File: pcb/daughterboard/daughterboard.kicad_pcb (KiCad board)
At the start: 2 copper layers, 220 x 50 mm, 71 parts, among them IC1 TLE94112ESXUMA1, IC2 TLE94112ESXUMA1, IC3 TLE94112ESXUMA1, IC4 TLE94112ESXUMA1, IC5 TLE94112ESXUMA1, IC6 TLE94112ESXUMA1, IC7 TLE94112ESXUMA1, J10 Conn_01x06_Socket, J11 Conn_01x06_Socket, J12 Conn_01x06_Socket, J13 Conn_01x06_Socket, J14 Conn_01x06_Socket, J15 Conn_01x06_Socket, J16 Conn_01x06_Socket, J17 Conn_01x06_Socket, J18 Conn_01x06_Socket, J19 Conn_01x06_Socket, J2 M20-7820646, J20 Conn_01x06_Socket, J21 Conn_01x06_Socket, J22 Conn_01x06_Socket, J23 Screw_Terminal_01x03, J3 Conn_01x06_Socket, J4 Conn_01x06_Socket, J5 Conn_01x06_Socket, J6 Conn_01x06_Socket, J7 Conn_01x06_Socket, J8 Conn_01x06_Socket, J9 Conn_01x06_Socket

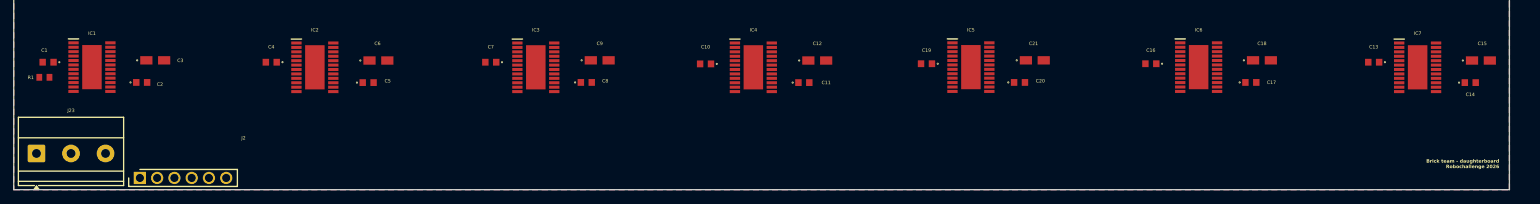
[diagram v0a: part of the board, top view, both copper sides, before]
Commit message: added power lines
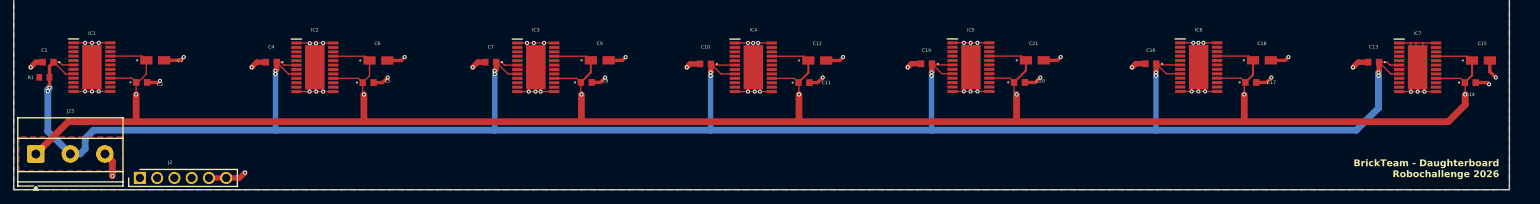
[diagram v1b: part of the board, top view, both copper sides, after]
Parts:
- moved J23 0.12 mm to (35.4, 147.3)
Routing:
- net +5.5V: track 0.00 -> 347.1 mm, vias 0 -> 7
- net +3.3V: track 0.00 -> 317.2 mm, vias 0 -> 14
- net GND: track 0.00 -> 298.4 mm, vias 0 -> 62
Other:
- board text added: "BrickTeam - Daughterboard Robochallenge 2026"
- board text removed: "Brick team - daughterboard Robochallenge 2026"

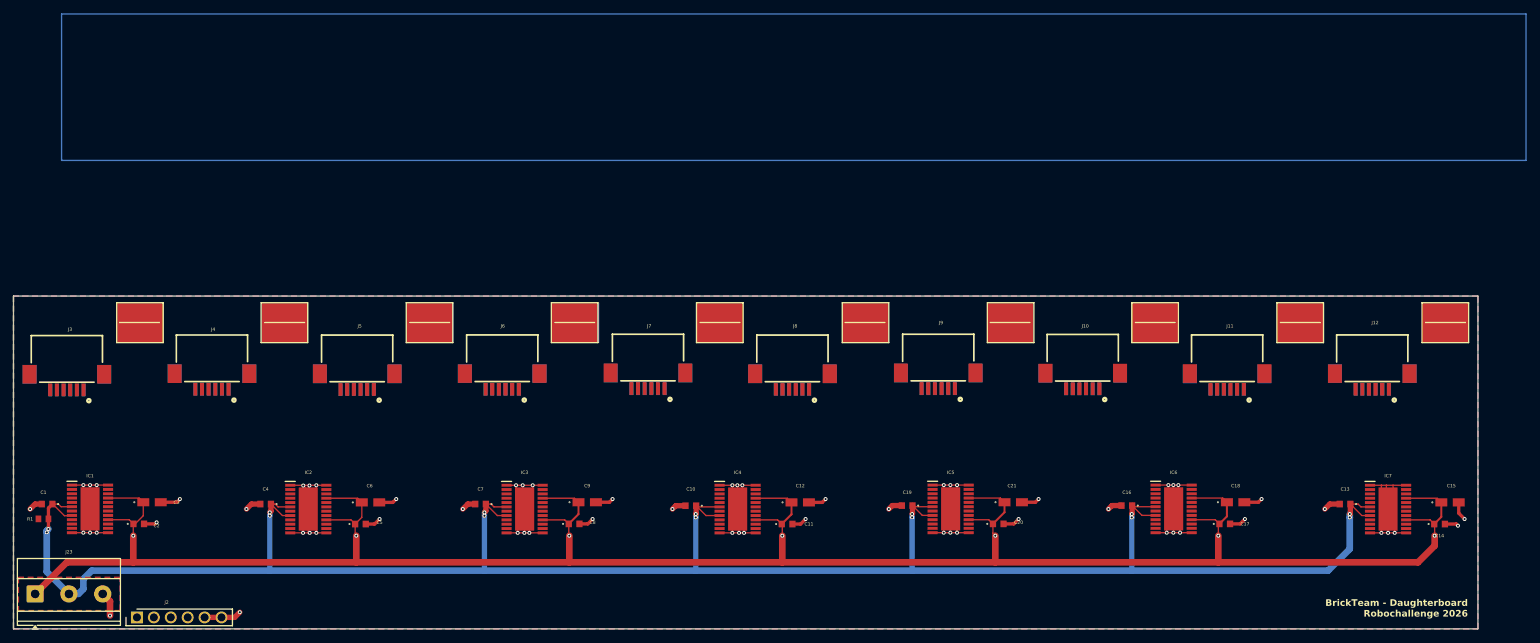
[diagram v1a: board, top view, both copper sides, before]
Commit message: Routed 10 motors and realised daisy-chain connection between drivers
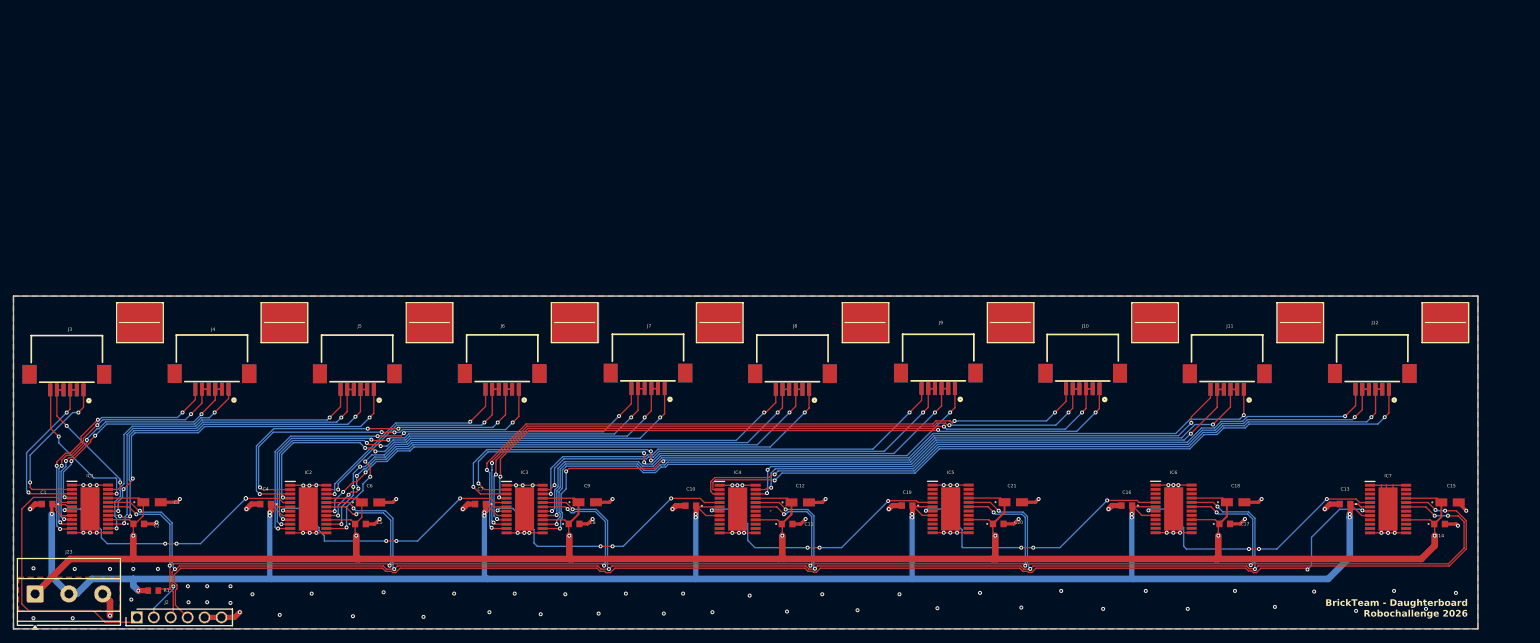
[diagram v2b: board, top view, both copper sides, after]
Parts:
- moved R1 19.7 mm to (53.1, 146.8), turned to 0 degrees
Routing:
- net /drivers1/SPI_SCLK: track 0.00 -> 329.2 mm, vias 0 -> 15
- net /drivers1/SPI_CS: track 0.00 -> 321.9 mm, vias 0 -> 14
- net /drivers2/SPI_MISO: track 0.00 -> 196.8 mm, vias 0 -> 2
- net PAD1_M9: track 0.00 -> 119.0 mm, vias 0 -> 2
- net PAD2_M9: track 0.00 -> 118.3 mm, vias 0 -> 2
- net PAD3_M9: track 0.00 -> 117.5 mm, vias 0 -> 2
- net PAD4_M9: track 0.00 -> 115.1 mm, vias 0 -> 4
- net PAD2_M10: track 0.00 -> 111.7 mm, vias 0 -> 2
- net PAD1_M10: track 0.00 -> 111.6 mm, vias 0 -> 2
- net PAD2_M8: track 0.00 -> 106.8 mm, vias 0 -> 4
- net PAD3_M8: track 0.00 -> 106.1 mm, vias 0 -> 4
- net PAD4_M8: track 0.00 -> 105.3 mm, vias 0 -> 4
- net PAD1_M8: track 0.00 -> 103.3 mm, vias 0 -> 4
- net PAD3_M10: track 0.00 -> 101.5 mm, vias 0 -> 2
- net PAD4_M10: track 0.00 -> 100.1 mm, vias 0 -> 3
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
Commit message: Finalized daughterboard pcb design 0 errors Verified every 3D model, footprint According to the schematic
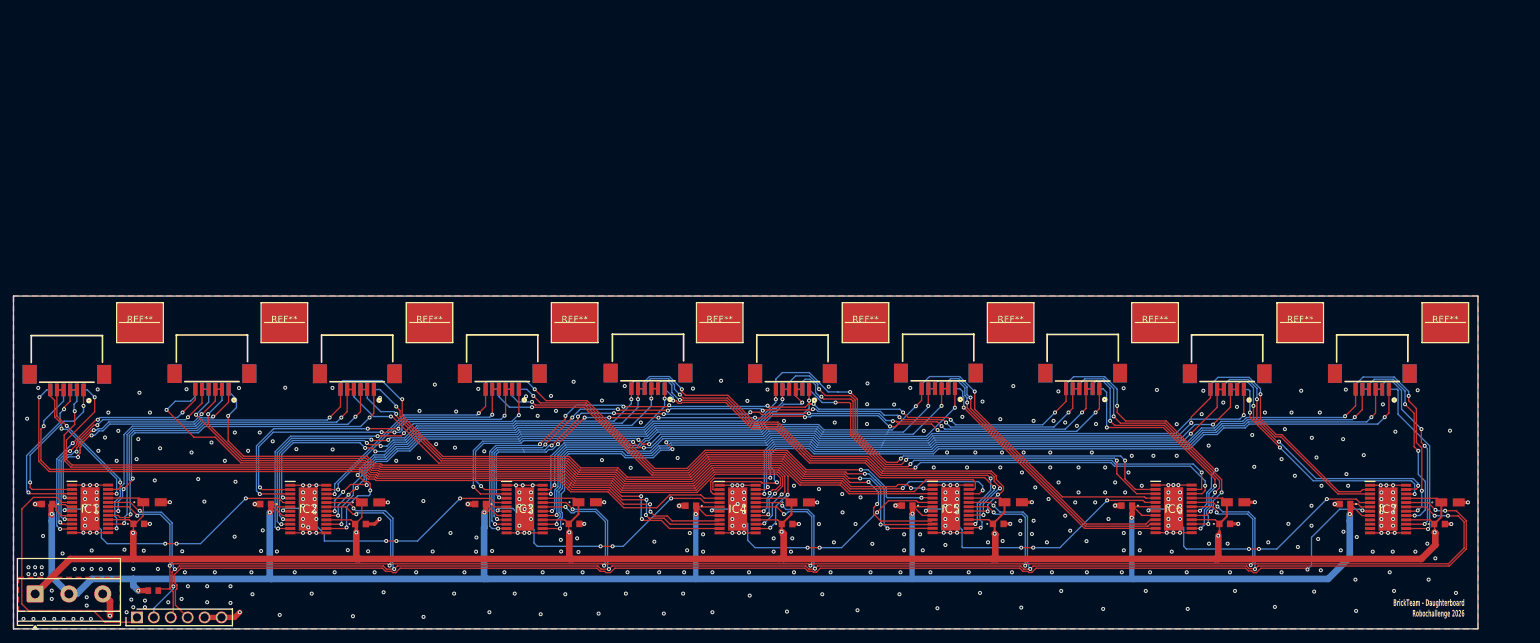
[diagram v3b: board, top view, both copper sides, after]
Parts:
- removed the ? at (160.1, 106.6) (x2)
- removed the ? at (247.2, 106.6)
- removed the ? at (225.5, 106.6)
- removed the ? at (247.3, 106.6)
- removed the ? at (116.6, 106.6)
- removed the ? at (203.7, 106.6)
- removed the ? at (181.9, 106.6) (x2)
- removed the ? at (94.7, 106.6)
- removed the ? at (138.3, 106.6)
- removed the ? at (72.8, 106.6)
- removed the ? at (72.9, 106.6)
- removed the REF** at (51.1, 106.6)
- added ?: , , F.Cu at (51.1, 106.6)
- added ?: , , F.Cu at (160.1, 106.6)
- added ?: , , F.Cu at (181.9, 106.6)
- added ?: , , F.Cu at (72.8, 106.6)
- added REF**: 6x7mm_F_pad, daughterboard:7x6mm_F_pad, F.Cu at (225.4, 106.6)
- added REF**: 6x7mm_F_pad, daughterboard:7x6mm_F_pad, F.Cu at (203.6, 106.6)
- added REF**: 6x7mm_F_pad, daughterboard:7x6mm_F_pad, F.Cu at (51.1, 106.6)
- added REF**: 6x7mm_F_pad, daughterboard:7x6mm_F_pad, F.Cu at (138.2, 106.6)
- added REF**: 6x7mm_F_pad, daughterboard:7x6mm_F_pad, F.Cu at (72.8, 106.6)
- added REF**: 6x7mm_F_pad, daughterboard:7x6mm_F_pad, F.Cu at (160.1, 106.6)
- added REF**: 6x7mm_F_pad, daughterboard:7x6mm_F_pad, F.Cu at (116.4, 106.6)
- added REF**: 6x7mm_F_pad, daughterboard:7x6mm_F_pad, F.Cu at (247.2, 106.6)
- added REF**: 6x7mm_F_pad, daughterboard:7x6mm_F_pad, F.Cu at (181.9, 106.6)
- added REF**: 6x7mm_F_pad, daughterboard:7x6mm_F_pad, F.Cu at (94.6, 106.6)
- IC1, IC2, IC3, IC4, IC5, IC6, IC7: footprint A_HANU_FOOTPRINTS:TLE94112ESXUMA1 -> driver_tle:SOP65P600X115-25N
- moved REF** 196.1 mm to (247.2, 112.3)
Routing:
- net PAD2_M11: track 1.00 -> 119.5 mm, vias 0 -> 3
- net PAD1_M11: track 0.00 -> 117.9 mm, vias 0 -> 1
- net PAD4_M11: track 0.00 -> 117.6 mm, vias 0 -> 3
- net PAD3_M11: track 1.00 -> 116.4 mm, vias 0 -> 3
- net PAD1_M12: track 0.17 -> 112.5 mm, vias 0 -> 3
- net PAD4_M12: track 0.00 -> 108.4 mm, vias 0 -> 3
- net PAD3_M12: track 1.00 -> 109.0 mm, vias 0 -> 3
- net PAD2_M12: track 1.00 -> 108.4 mm, vias 0 -> 3
- net PAD4_M13: track 0.00 -> 104.2 mm, vias 0 -> 3
- net PAD3_M13: track 1.00 -> 104.8 mm, vias 0 -> 1
- net PAD1_M13: track 0.00 -> 100.8 mm, vias 0 -> 3
- net PAD2_M13: track 1.00 -> 97.3 mm, vias 0 -> 1
- net PAD2_M14: track 1.00 -> 80.4 mm, vias 0 -> 3
- net PAD1_M14: track 0.00 -> 78.5 mm, vias 0 -> 3
- net PAD3_M14: track 1.00 -> 78.6 mm, vias 0 -> 3
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
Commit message: Final touches for the PCB order Added MPN, Description, checked footprints and 3D models Finished the BOM
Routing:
- net PAD4_M8: track 108.9 -> 109.6 mm
- net PAD3_M8: track 109.3 -> 109.8 mm
- net GND: vias 450 -> 416
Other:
- board text added: "BRICKTEAM 2026"
- board text removed: "BrickTeam - Daughterboard Robochallenge 2026"

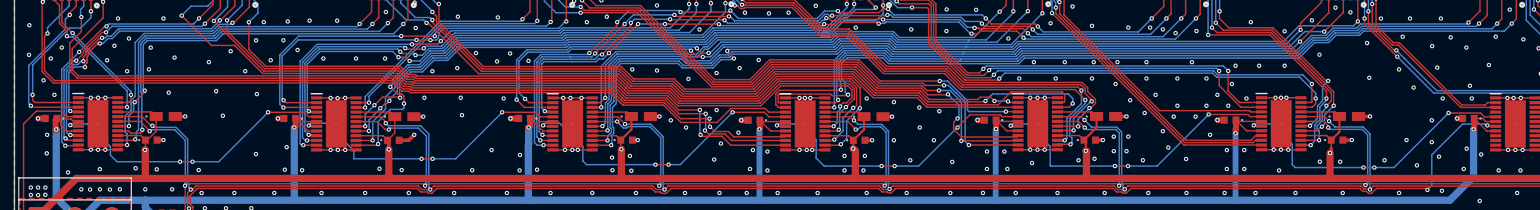
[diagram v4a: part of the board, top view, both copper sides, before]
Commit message: fixed via positioning errors
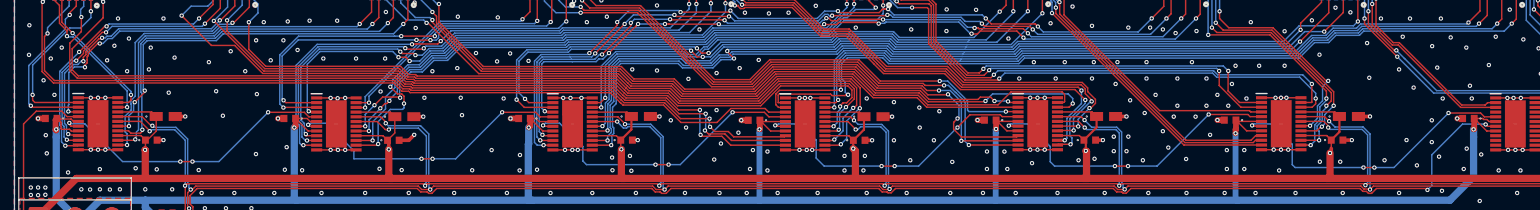
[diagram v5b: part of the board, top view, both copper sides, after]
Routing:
- net PAD2_M5: track 74.3 -> 75.1 mm
- net GND: vias 416 -> 417

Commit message: modified motor connectors
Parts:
- removed the ? at (203.6, 106.6)
- removed the ? at (51.1, 106.6)
- removed the ? at (160.1, 106.6)
- removed the ? at (116.4, 106.6)
- removed the ? at (225.4, 106.6)
- removed the ? at (72.8, 106.6)
- removed J23: Screw_Terminal_01x03, TerminalBlock_Phoenix:TerminalBlock_Phoenix_MKDS-1,5-3-5.08_1x03_P5.08mm_Horizontal
- removed the REF** at (225.4, 106.6)
- removed the REF** at (203.6, 106.6)
- removed the REF** at (138.2, 106.6)
- removed the REF** at (72.8, 106.6)
- removed the REF** at (160.1, 106.6)
- removed the REF** at (116.4, 106.6)
- removed the REF** at (247.2, 106.6)
- removed the REF** at (181.9, 106.6)
- removed the REF** at (94.6, 106.6)
- added ?: , , F.Cu at (181.8, 106.6)
- added ? (x2): , , F.Cu at (72.8, 106.6)
- added ?: , , F.Cu at (94.6, 106.6)
- added ? (x2): , , F.Cu at (203.6, 106.6)
- added ? (x2): , , F.Cu at (116.4, 106.6)
- added ? (x2): , , F.Cu at (160.1, 106.6)
- added ?: , , F.Cu at (51.0, 106.6)
- added ? (x2): , , F.Cu at (225.4, 106.6)
- added ?: , , F.Cu at (138.3, 106.6)
- added ?: , , F.Cu at (247.2, 106.6)
- added J1: Screw_Terminal_01x03, TerminalBlock_Phoenix:TerminalBlock_Phoenix_MKDS-1,5-3-5.08_1x03_P5.08mm_Horizontal, F.Cu at (35.3, 147.3)
- J10, J11, J12, J13, J14, J15, J16, J17, J18, J19, J20, J21, J22, J3, J4, J5, J6, J7, J8, J9: value Conn_01x06_Socket -> FFC3B11-06-T; footprint 52207-0633:52207-0633 -> FFC3B11_06_T:GCT_FFC3B11-06-T
- moved J10 2.85 mm to (192.7, 113.7)
- moved J11 2.85 mm to (214.4, 113.8)
- moved J12 2.85 mm to (236.2, 113.8)
- moved J13 2.85 mm to (40.1, 113.8)
- moved J14 2.85 mm to (61.9, 113.8)
- moved J15 2.85 mm to (83.7, 113.8)
- moved J16 2.85 mm to (105.5, 113.8)
- moved J17 2.85 mm to (127.4, 113.7)
- moved J18 2.85 mm to (149.1, 113.8)
- moved J19 2.85 mm to (171.0, 113.7)
- moved J20 2.85 mm to (192.7, 113.7)
- moved J21 2.85 mm to (214.4, 113.8)
- moved J22 2.85 mm to (236.2, 113.8)
- moved J4 2.85 mm to (61.9, 113.8)
- moved J5 2.85 mm to (83.7, 113.8)
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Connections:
- J10 pad 1: PAD1_M8 -> PAD4_M8
- J10 pad 2: PAD2_M8 -> PAD3_M8
- J10 pad 3: PAD2_M8 -> PAD3_M8
- J10 pad 4: PAD3_M8 -> PAD2_M8
- J10 pad 5: PAD3_M8 -> PAD2_M8
- J10 pad 6: PAD4_M8 -> PAD1_M8
- J11 pad 1: PAD1_M9 -> PAD4_M9
- J11 pad 2: PAD2_M9 -> PAD3_M9
- J11 pad 3: PAD2_M9 -> PAD3_M9
- J11 pad 4: PAD3_M9 -> PAD2_M9
- J11 pad 5: PAD3_M9 -> PAD2_M9
- J11 pad 6: PAD4_M9 -> PAD1_M9
- J12 pad 1: PAD1_M10 -> PAD4_M10
- J12 pad 2: PAD2_M10 -> PAD3_M10
- J12 pad 3: PAD2_M10 -> PAD3_M10
- J12 pad 4: PAD3_M10 -> PAD2_M10
- J12 pad 5: PAD3_M10 -> PAD2_M10
- J12 pad 6: PAD4_M10 -> PAD1_M10
- J13 pad 1: PAD1_M11 -> PAD4_M11
- J13 pad 2: PAD2_M11 -> PAD3_M11
- J13 pad 3: PAD2_M11 -> PAD3_M11
- J13 pad 4: PAD3_M11 -> PAD2_M11
- J13 pad 5: PAD3_M11 -> PAD2_M11
- J13 pad 6: PAD4_M11 -> PAD1_M11
- J14 pad 1: PAD1_M12 -> PAD4_M12
- J14 pad 2: PAD2_M12 -> PAD3_M12
- J14 pad 3: PAD2_M12 -> PAD3_M12
- J14 pad 4: PAD3_M12 -> PAD2_M12
- J14 pad 5: PAD3_M12 -> PAD2_M12
- J14 pad 6: PAD4_M12 -> PAD1_M12
- J15 pad 1: PAD1_M13 -> PAD4_M13
- J15 pad 2: PAD2_M13 -> PAD3_M13
- J15 pad 3: PAD2_M13 -> PAD3_M13
- J15 pad 4: PAD3_M13 -> PAD2_M13
- J15 pad 5: PAD3_M13 -> PAD2_M13
- J15 pad 6: PAD4_M13 -> PAD1_M13
- J16 pad 1: PAD1_M14 -> PAD4_M14
- J16 pad 2: PAD2_M14 -> PAD3_M14
- J16 pad 3: PAD2_M14 -> PAD3_M14
- J16 pad 4: PAD3_M14 -> PAD2_M14
- J16 pad 5: PAD3_M14 -> PAD2_M14
- J16 pad 6: PAD4_M14 -> PAD1_M14
- J17 pad 1: PAD1_M15 -> PAD4_M15
- J17 pad 2: PAD2_M15 -> PAD3_M15
- J17 pad 3: PAD2_M15 -> PAD3_M15
- J17 pad 4: PAD3_M15 -> PAD2_M15
- J17 pad 5: PAD3_M15 -> PAD2_M15
- J17 pad 6: PAD4_M15 -> PAD1_M15
- J18 pad 1: PAD1_M16 -> PAD4_M16
- J18 pad 2: PAD2_M16 -> PAD3_M16
- J18 pad 3: PAD2_M16 -> PAD3_M16
- J18 pad 4: PAD3_M16 -> PAD2_M16
- J18 pad 5: PAD3_M16 -> PAD2_M16
- J18 pad 6: PAD4_M16 -> PAD1_M16
- J19 pad 1: PAD1_M17 -> PAD4_M17
- J19 pad 2: PAD2_M17 -> PAD3_M17
- J19 pad 3: PAD2_M17 -> PAD3_M17
- J19 pad 4: PAD3_M17 -> PAD2_M17
- J19 pad 5: PAD3_M17 -> PAD2_M17
- J19 pad 6: PAD4_M17 -> PAD1_M17
- J20 pad 1: PAD1_M18 -> PAD4_M18
- J20 pad 2: PAD2_M18 -> PAD3_M18
- J20 pad 3: PAD2_M18 -> PAD3_M18
- J20 pad 4: PAD3_M18 -> PAD2_M18
- J20 pad 5: PAD3_M18 -> PAD2_M18
- J20 pad 6: PAD4_M18 -> PAD1_M18
- J21 pad 1: PAD1_M19 -> PAD4_M19
- J21 pad 2: PAD2_M19 -> PAD3_M19
- J21 pad 3: PAD2_M19 -> PAD3_M19
- J21 pad 4: PAD3_M19 -> PAD2_M19
- J21 pad 5: PAD3_M19 -> PAD2_M19
- J21 pad 6: PAD4_M19 -> PAD1_M19
- J22 pad 1: PAD1_M20 -> PAD4_M20
- J22 pad 2: PAD2_M20 -> PAD3_M20
- J22 pad 3: PAD2_M20 -> PAD3_M20
- J22 pad 4: PAD3_M20 -> PAD2_M20
- J22 pad 5: PAD3_M20 -> PAD2_M20
- J22 pad 6: PAD4_M20 -> PAD1_M20
- J3 pad 1: PAD1_M1 -> PAD4_M1
- J3 pad 2: PAD2_M1 -> PAD3_M1
- J3 pad 3: PAD2_M1 -> PAD3_M1
- J3 pad 4: PAD3_M1 -> PAD2_M1
- J3 pad 5: PAD3_M1 -> PAD2_M1
- J3 pad 6: PAD4_M1 -> PAD1_M1
- J4 pad 1: PAD1_M2 -> PAD4_M2
- J4 pad 2: PAD2_M2 -> PAD3_M2
- J4 pad 3: PAD2_M2 -> PAD3_M2
- J4 pad 4: PAD3_M2 -> PAD2_M2
- J4 pad 5: PAD3_M2 -> PAD2_M2
- J4 pad 6: PAD4_M2 -> PAD1_M2
- J5 pad 1: PAD1_M3 -> PAD4_M3
- J5 pad 2: PAD2_M3 -> PAD3_M3
- J5 pad 3: PAD2_M3 -> PAD3_M3
- J5 pad 4: PAD3_M3 -> PAD2_M3
- J5 pad 5: PAD3_M3 -> PAD2_M3
- J5 pad 6: PAD4_M3 -> PAD1_M3
- J6 pad 1: PAD1_M4 -> PAD4_M4
- J6 pad 2: PAD2_M4 -> PAD3_M4
- J6 pad 3: PAD2_M4 -> PAD3_M4
- J6 pad 4: PAD3_M4 -> PAD2_M4
- J6 pad 5: PAD3_M4 -> PAD2_M4
- J6 pad 6: PAD4_M4 -> PAD1_M4
- J7 pad 1: PAD1_M5 -> PAD4_M5
- J7 pad 2: PAD2_M5 -> PAD3_M5
- J7 pad 3: PAD2_M5 -> PAD3_M5
- J7 pad 4: PAD3_M5 -> PAD2_M5
- J7 pad 5: PAD3_M5 -> PAD2_M5
- J7 pad 6: PAD4_M5 -> PAD1_M5
- J8 pad 1: PAD1_M6 -> PAD4_M6
- J8 pad 2: PAD2_M6 -> PAD3_M6
- J8 pad 3: PAD2_M6 -> PAD3_M6
- J8 pad 4: PAD3_M6 -> PAD2_M6
- J8 pad 5: PAD3_M6 -> PAD2_M6
- J8 pad 6: PAD4_M6 -> PAD1_M6
- J9 pad 1: PAD1_M7 -> PAD4_M7
- J9 pad 2: PAD2_M7 -> PAD3_M7
- J9 pad 3: PAD2_M7 -> PAD3_M7
- J9 pad 4: PAD3_M7 -> PAD2_M7
- J9 pad 5: PAD3_M7 -> PAD2_M7
- J9 pad 6: PAD4_M7 -> PAD1_M7
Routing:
- net GND: track 271.4 -> 350.1 mm, vias 417 -> 446
- net PAD1_M19: track 35.1 -> 37.0 mm
- net PAD2_M20: track 30.6 -> 32.4 mm
- net PAD1_M20: track 30.8 -> 32.5 mm
- net PAD3_M17: track 43.8 -> 45.5 mm
- net PAD1_M17: track 45.4 -> 47.1 mm
- net PAD3_M20: track 30.0 -> 31.7 mm
- net PAD2_M17: track 46.1 -> 47.8 mm
- net PAD2_M19: track 33.7 -> 35.1 mm
- net PAD1_M18: track 40.1 -> 41.5 mm
- net PAD3_M18: track 39.9 -> 41.2 mm
- net PAD2_M15: track 70.5 -> 71.8 mm
- net PAD2_M18: track 40.7 -> 41.9 mm
- net PAD1_M15: track 72.1 -> 73.2 mm
- net PAD3_M19: track 40.6 -> 41.6 mm
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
